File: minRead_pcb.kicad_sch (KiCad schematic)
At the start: 154 parts, among them J1 USB_C_Receptacle, J2 FH34SRJ-24S-0.5SH_50_, J3 FH34SRJ-6S-0.5SH_50_, J4 FH34SRJ-6S-0.5SH_50_, J5 Conn_01x02, J6 PPPC062LJBN-RC, J7 Micro_SD_Card, Q1 FS8205A, Q12 MMBT3904, Q13 MMBT3904, Q14 AO3419, Q15 MMBT3906, Q16 MMBT3906, Q17 MMBT3904, Q3 AO3419, Q4 BSS138, Q5 BSS138, Q6 BSS138, Q7 AO3419, Q8 AO3419, Q9 BSS138, SW1 SW_Push, SW10 SW_Push, SW11 SW_Push, SW2 SW_Push, SW3 SW_Push, SW4 SW_Push, SW5 SW_Push, SW6 SW_Push, SW7 SW_Push, SW8 SW_Push, SW9 SW_Push, U1 TPD4E1U06DBVR, U10 AP3031KTR, U2 TPS2116DRL, U3 AP2112K-3.3, U4 ESP32-S3-WROOM-1, U5 DW01A, U6 TPD4E1U06DBVR, U7 MCP73832-2-OT, U8 TPD4E1U06DBVR, U9 TPD4E1U06DBVR

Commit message: Schematic/PCB: finalize changes and layout progress
C- -> pin 1; W- -> pin 2; GND -> pin 3.

Schematic mostly finalized. 74 inverter used instead of PNP/NPN. ESP32 pinout configured. Components semi-optimally laid out; remaining traces TBD.
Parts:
- removed Q16: MMBT3906, Package_TO_SOT_SMD:SOT-23_Handsoldering, symbol Transistor_BJT:MMBT3906
- removed Q17: MMBT3904, Package_TO_SOT_SMD:SOT-23_Handsoldering, symbol Transistor_BJT:MMBT3904
- removed R47, R48: 18k, Resistor_SMD:R_0805_2012Metric_Pad1.20x1.40mm_HandSolder, symbol Device:R
- removed U7: MCP73832-2-OT, Package_TO_SOT_SMD:SOT-23-5, symbol Battery_Management:MCP73832-2-OT
- added R62: 10k, Resistor_SMD:R_0805_2012Metric_Pad1.20x1.40mm_HandSolder, symbol Device:R
- added R63, R64: 100, Resistor_SMD:R_0805_2012Metric_Pad1.20x1.40mm_HandSolder, symbol Device:R
- added R65: 33, Resistor_SMD:R_0805_2012Metric_Pad1.20x1.40mm_HandSolder, symbol Device:R
- added U11: TP4056-42-ESOP8, Package_SO:SOIC-8-1EP_3.9x4.9mm_P1.27mm_EP2.41x3.3mm_ThermalVias, symbol Battery_Management:TP4056-42-ESOP8
- added U12: 74LVC1G04, Package_TO_SOT_SMD:SOT-23-5_HandSoldering, symbol 74xGxx:74LVC1G04
- added U7: TPD4E1U06DBVR, Package_TO_SOT_SMD:SOT-23-6_Handsoldering, symbol TPD4E1U06DBVR:TPD4E1U06DBVR
- C2, C3: value 4.7u -> 10u
- C24: value 2.2n -> 100n
- D2: footprint LED_THT:LED_D3.0mm -> LED_SMD:LED_1206_3216Metric_Pad1.42x1.75mm_HandSolder
- R6: value 10k -> 12k
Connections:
- net CHG_STATUS is gone; now on net BAT_MONIT: U4.12 (IO8)
- net LED_PWR is gone; now on an unnamed net: U4.10 (IO17)
- net WARM_TOGGLE is gone; now on an unnamed net: U4.6 (IO6)
- net 3V3: now also C24.1, U12.5 (VCC)
- net BAT_MONIT: no longer U4.4 (IO4)
- net BUTTON_ADC_2: now also U4.4 (IO4); no longer U4.38 (IO2)
- net C-: now also Q6.3 (D), R49.1; no longer Q5.3 (D), R50.1
- net COLOR_SEL: now also U4.35 (IO42), U12.2
- net COLOR_SEL_INV: now also U12.4; no longer C24.1
- net ESP32_EN: now also R63.2; no longer SW11.2
- net ESP32_IO0: now also R64.2; no longer SW6.2
- net GND: now also C29.2, D8.3 (common), U11.1 (TEMP), U11.3 (GND), U11.9 (EPAD), U12.3 (GND), U7.2; no longer C29.1, D8.2 (common)
- net ISO_GATE: now also Q12.3 (C), Q9.1 (G), R42.2, R43.2
- net LED_ACTIVATE: now also U4.34 (IO41)
- net P+: now also U11.5 (BAT)
- net PWM_LED: now also U4.33 (IO40); no longer U4.5 (IO5)
- net PWR_BUTTON: now also C29.1, U4.11 (IO18), R62.2; no longer SW10.1, U4.15 (IO3)
- net RX: no longer J6.6, U9.4
- net SD_CLK: now also U9.1
- net SD_CMD: now also U9.3
- net SD_DAT0: now also U1.6; no longer U1.4
- net SD_DAT1: now also U1.4; no longer U1.3
- net SD_DAT2: now also U1.3; no longer U1.1
- net SD_DAT3: now also U1.1; no longer U1.6
- net TX: no longer J6.11, U8.3
- net USB_STAT: now also U4.17 (IO9)
- net USB_VBUS: now also U11.4 (V_{CC}), U11.8 (CE)
- net W-: now also D8.2 (A2), Q5.3 (D), R50.1; no longer D8.3 (A2), Q6.3 (D), R49.1
- net at R59.2: now also U11.7 (~{CHRG})
- net at R21.1: no longer U4.35 (IO42)
- net at R23.1: now also U4.8 (IO15); no longer U4.33 (IO40)
- net at R29.2: now also U4.20 (IO12); no longer U4.17 (IO9)
- net at R6.1: now also U11.2 (PROG)
- net at R33.2: now also U4.24 (IO47); no longer U4.21 (IO13)
- net at R22.1: now also U4.9 (IO16); no longer U4.34 (IO41)
- net at R26.1: now also U4.5 (IO5); no longer U4.25 (IO48)
- net at R25.1: now also U4.7 (IO7); no longer U4.32 (IO39)
- net at R24.1: no longer U4.31 (IO38)
- net at R32.2: now also U4.23 (IO21); no longer U4.20 (IO12)
- net at R34.2: now also U4.25 (IO48); no longer U4.22 (IO14)
- net at R30.2: now also U4.21 (IO13); no longer U4.18 (IO10)
- net at R31.2: now also U4.22 (IO14); no longer U4.19 (IO11)
- net EPD_MOSI renamed SPI_MOSI
- net EPD_SCK renamed SPI_SCK
- net INT renamed TP_INT
- net TP_INT: now also U4.18 (IO10), U7.1
- net RST renamed TP_RST
- net TP_RST: now also U4.19 (IO11), U7.3
- net SCL renamed I2C_SCL
- net I2C_SCL: now also U4.32 (IO39), U7.6
- net SDA renamed I2C_SDA
- net I2C_SDA: now also U4.31 (IO38), U7.4
- removed net UNUSED_GPIO_15: J6.5, U4.8 (IO15), U9.3
- removed net UNUSED_GPIO_16: J6.10, U4.9 (IO16), U9.6
- removed net UNUSED_GPIO_45: J6.3, U4.26 (IO45), U9.1
- removed net UNUSED_GPIO_46: J6.9, U4.16 (IO46), U8.6
- removed net UNUSED_GPIO_47: J6.4, U4.24 (IO47), U8.1
- new net: R62.1, SW10.1
- new net: R63.1, SW11.2
- new net: R65.2, U4.38 (IO2)
- new net: R64.1, SW6.2
- new net SPI_MISO: R65.1
- new net UNUSED_GPIO_3: U4.15 (IO3)
- no-connect marks 13 -> 15
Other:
- note added: "1u cap placed at ESP32"
- note added: "2.2n cap placed near ESP32"
- note added: "R6 12kohm -> 100mA charge rate"
- note removed: "10kohm -> 100mA charge rate"
- note removed: "Taken from"
- note removed: "https://tinyurl.com/4bm2ynx9"
- moved on the sheet: C2, C27, C8, D2, H1, H2, H3, H4, J4, R21, R22, R23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

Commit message: finished layout, schematic, tbd on next steps for review
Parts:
- SW6: footprint Button_Switch_THT:SW_PUSH_6mm -> Button_Switch_THT:SW_PUSH_1P1T_6x3.5mm_H4.3_APEM_MJTP1243; now fitted
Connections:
- net 3V3: now also J6.7; no longer J6.12
- net C-: now also J6.11; no longer J6.2
- net GND: now also J6.12
- net I2C_SCL: now also J6.10, U8.3
- net I2C_SDA: now also J6.4, U8.4
- net LED_SW: now also J6.5; no longer J6.7
- net SPI_MISO: now also J6.3, U8.1
- net SPI_MOSI: now also J6.8, U9.4
- net SPI_SCK: now also J6.2, U9.6
- net UNUSED_GPIO_3: now also J6.9, U8.6
- net W-: now also J6.6; no longer J6.8
- no-connect marks 15 -> 14

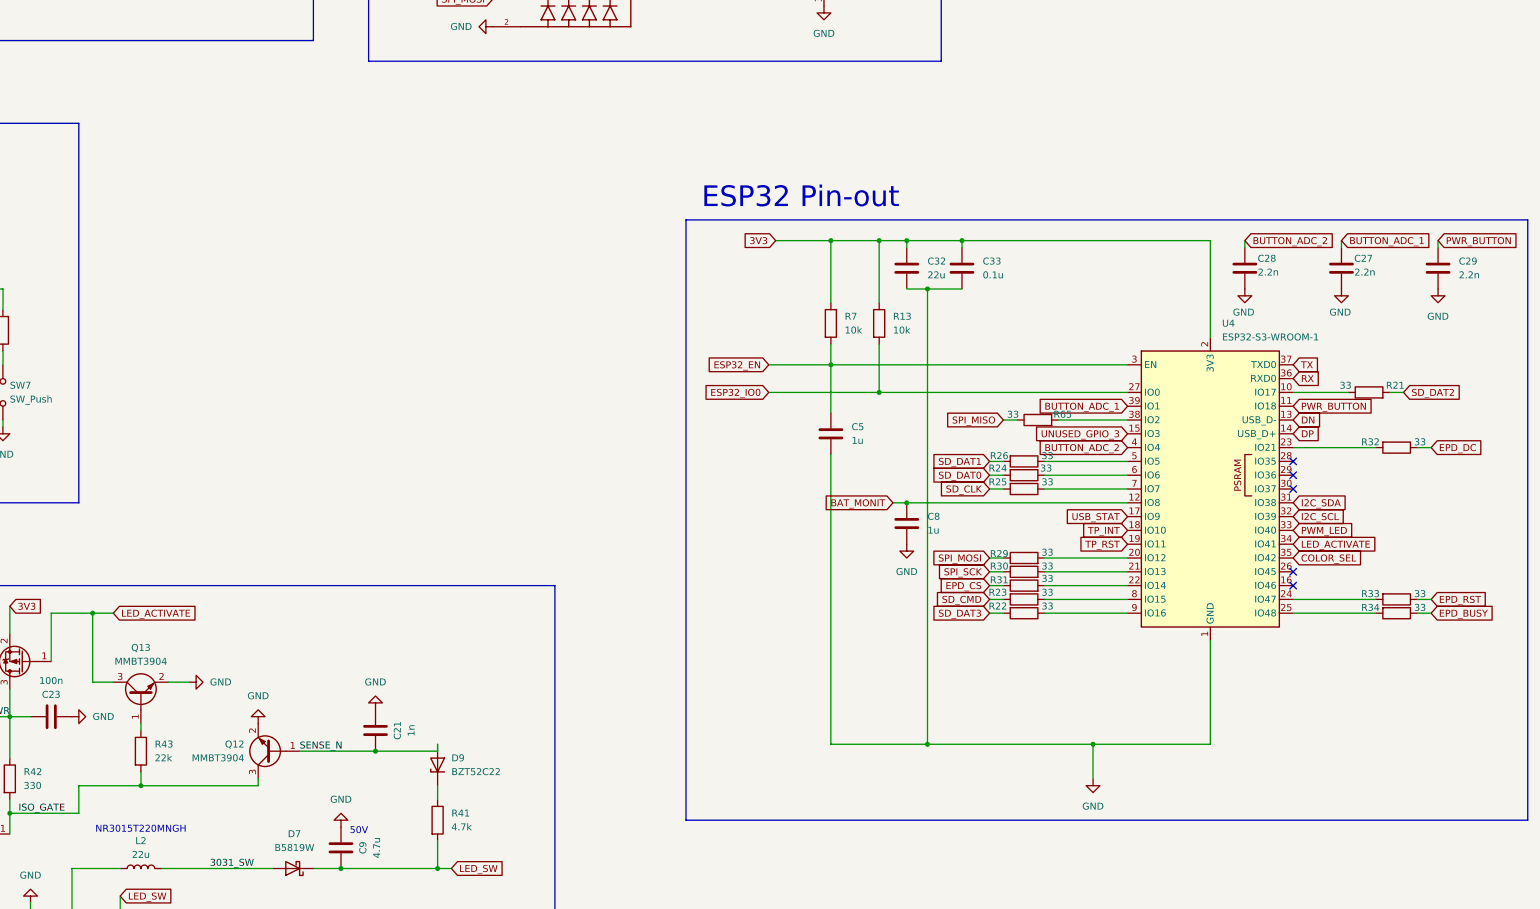
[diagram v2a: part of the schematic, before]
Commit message: removed (most) vias on pads, added rtc ds3231, added TPs for UART TX/RX TBD: trace spacing, further review of habits
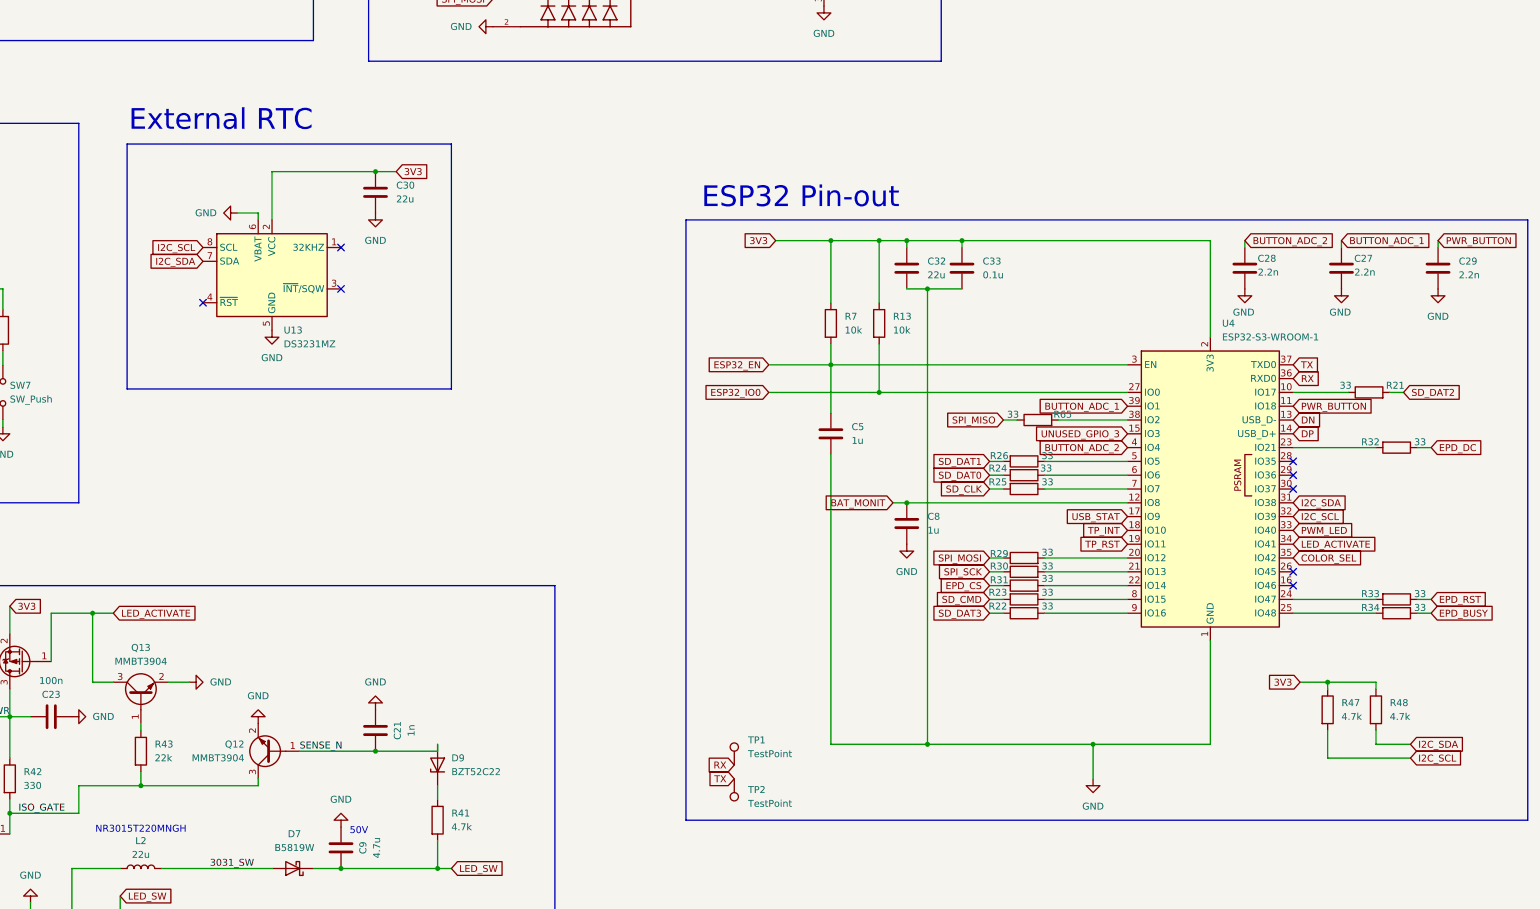
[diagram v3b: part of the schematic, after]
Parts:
- added C30: 22u, Capacitor_SMD:C_0805_2012Metric_Pad1.18x1.45mm_HandSolder, symbol Device:C
- added R47, R48: 4.7k, Resistor_SMD:R_0805_2012Metric_Pad1.20x1.40mm_HandSolder, symbol Device:R
- added TP1, TP2: TestPoint, TestPoint:TestPoint_Pad_1.0x1.0mm, symbol Connector:TestPoint
- added U13: DS3231MZ, Package_SO:SOIC-8_3.9x4.9mm_P1.27mm, symbol Timer_RTC:DS3231MZ
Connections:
- net 3V3: now also C30.1, R47.1, R48.1, U13.2 (VCC)
- net GND: now also C30.2, U13.5 (GND), U13.6 (VBAT)
- net I2C_SCL: now also R47.2, U13.8 (SCL)
- net I2C_SDA: now also R48.2, U13.7 (SDA)
- net RX: now also TP1.1
- net TX: now also TP2.1
- no-connect marks 14 -> 17
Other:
- note added: "External RTC"

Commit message: added voltage divider to 3031 reduced led driver passives size to 0603
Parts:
- added R66: 680k, Resistor_SMD:R_0603_1608Metric_Pad0.98x0.95mm_HandSolder, symbol Device:R
- added R67: 1M, Resistor_SMD:R_0603_1608Metric_Pad0.98x0.95mm_HandSolder, symbol Device:R
- C12, C21, C23, C24: footprint Capacitor_SMD:C_0805_2012Metric_Pad1.18x1.45mm_HandSolder -> Capacitor_SMD:C_0603_1608Metric_Pad1.08x0.95mm_HandSolder
- R17, R37, R39, R40, R41, R42, R43, R44, R45, R46, R49, R50, R52: footprint Resistor_SMD:R_0805_2012Metric_Pad1.20x1.40mm_HandSolder -> Resistor_SMD:R_0603_1608Metric_Pad0.98x0.95mm_HandSolder
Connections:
- net GND: now also R67.2
- net LED_SW: now also R66.1; no longer U10.5 (OV)
- new net OVP: R66.2, R67.1, U10.5 (OV)

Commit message: updated silkscreen reference spacing updated silkscreen of graphics still need to do more of above added netclass for switching nodes and high voltage output caps, enforced 3mm clearance
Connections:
- net EINK_SW: now reaches C11.2, D5.2 (A), L1.1, Q4.3 (D)
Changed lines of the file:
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@@
 		)
 	)
-	(label "3031_SW"
-		(at 289.56 312.42 0)
-		(effects
-			(font
-				(size 1.27 1.27)
-			)
-			(justify left bottom)
-		)
-	)
 	(label "LATCH_PWR"
 		(at 278.13 248.92 180)
@@
 		)
 	)
-	(label "3031_SW"
-		(at 314.96 276.86 0)
-		(effects
-			(font
-				(size 1.27 1.27)
-			)
-			(justify left bottom)
-		)
-	)
 	(label "GDR"
 		(at 140.97 251.46 180)
@@
 		)
 	)
+	(global_label "3031_SW"
+		(shape input)
+		(at 318.77 276.86 90)
+		(fields_autoplaced yes)
+		(effects
+			(font
+				(size 1.27 1.27)
+			)
+			(justify left)
+		)
+		(property "Intersheetrefs" "${INTERSHEET_REFS}"
+			(at 318.77 265.4083 90)
+			(effects
+				(font
+					(size 1.27 1.27)
+				)
+				(justify left)
+				(hide yes)
+			)
+		)
+	)
 	(global_label "COLOR_SEL"
 		(shape input)
@@
 		)
 	)
+	(global_label "3031_SW"
+		(shape input)
+		(at 289.56 312.42 180)
+		(fields_autoplaced yes)
+		(effects
+			(font
+				(size 1.27 1.27)
+			)
+			(justify right)
+		)
+		(property "Intersheetrefs" "${INTERSHEET_REFS}"
+			(at 278.1083 312.42 0)
+			(effects
+				(font
+					(size 1.27 1.27)
+				)
+				(justify right)
+				(hide yes)
+			)
+		)
+	)
 	(global_label "3V3"
 		(shape input)
@@
 				(hide yes)
 			)
+		)
+	)
+	(global_label "EINK_SW"
+		(shape input)
+		(at 66.04 294.64 0)
+		(fields_autoplaced yes)
+		(effects
+			(font
+				(size 1.27 1.27)
+			)
+			(justify left)
+		)
+		(property "Intersheetrefs" "${INTERSHEET_REFS}"
+			(at 77.008 294.64 0)
+			(effects
+				(font
+					(size 1.27 1.27)
+				)
+				(justify left)
+				(hide yes)
+			)

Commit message: - added LED_ACTIVATE net to proper spot for transistor latch mechanism - added moved 1M ground bleed to SENSE_N instead of 3V3 - removed SPI signals from external header - added GPIO3, GPIO46, GPIO2 to external header with 33ohm series resistors - added P+ to external header with TS05D ESD protection diode - replaced inductor with molded inductor for LED driver (noise reduction) - replaced output cap for LED driver with tantalum cap (noise reduction) - cleaned up unconnected nets - todo: silkscreen (again), EMI stuff, etc
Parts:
- added CR3: TSD05CDYFR, Diode_SMD:D_SOD-323_HandSoldering, symbol TSD05CDYFR:TSD05CDYFR
- added R68, R69: 33, Resistor_SMD:R_0805_2012Metric_Pad1.20x1.40mm_HandSolder, symbol Device:R
- C30: value 22u -> 0.1u
- C9: value 4.7u -> 1u; footprint Capacitor_SMD:C_0805_2012Metric_Pad1.18x1.45mm_HandSolder -> Capacitor_Tantalum_SMD:CP_EIA-3528-21_Kemet-B_HandSolder; symbol Device:C -> Device:C_Polarized
- L2: value 22u -> 4.7u; footprint srn3010C-100m:IND_SRN3010C-100M -> Inductor_SMD:L_1008_2520Metric_Pad1.43x2.20mm_HandSolder
- R40: value 10k -> 100k
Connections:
- net 3V3: now also U13.6 (VBAT); no longer R17.1, U13.2 (VCC)
- net GND: now also C9.2, U13.2 (VCC), CR3.2 (GND); no longer C9.1, U13.6 (VBAT)
- net LED_ACTIVATE: now also Q9.2 (S), R39.1
- net LED_SW: now also C9.1; no longer C9.2
- net P+: now also J6.8, CR3.1 (I/O)
- net SENSE_N: now also R17.1
- net SPI_MISO: now also U4.26 (IO45); no longer J6.3, R65.1, U8.1
- net SPI_MOSI: no longer J6.8, U9.4
- net SPI_SCK: no longer J6.2, U9.6
- net UNUSED_GPIO_3: now also R68.1; no longer U4.15 (IO3)
- net at U4.16 (IO46): now also R69.1
- new net: R68.2, U4.15 (IO3)
- new net UNUSED_GPIO_2: J6.3, R65.1, U8.1
- new net UNUSED_GPIO_46: J6.2, R69.2, U9.6
- no-connect marks 17 -> 16
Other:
- note added: "50V Tantalum"
- note added: "74479325207247"
- note removed: "50V"
- moved on the sheet: C30, D9, R17, R65

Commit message: Swap AP3031 -> TPS923610DRLR, add SW net-class
- add SW net-class and assignments (3031_SW, LED_SW, EINK_SW) in .kicad_pro
- remove AP3031 symbol library (AP3031.kicad_sym/.bak) + sym-lib-table entry
- add TPS923610DRLR: symbol, footprint (U_DRL0006A_6L_TEX + L/M variants),
  and SOT563 3D model; registered in sym-lib-table and fp-lib-table
- schematic/board design updates
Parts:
- removed C9: 1u, Capacitor_Tantalum_SMD:CP_EIA-3528-21_Kemet-B_HandSolder, symbol Device:C_Polarized
- removed D7: B5819W, Diode_SMD:D_SOD-123, symbol Diode:MBR0540
- removed D9: BZT52C22, Diode_SMD:D_SOD-123F, symbol Diode:BZT52Bxx
- removed Q12, Q13: MMBT3904, Package_TO_SOT_SMD:SOT-23_Handsoldering, symbol Transistor_BJT:MMBT3904
- removed Q14: AO3419, Package_TO_SOT_SMD:SOT-23_Handsoldering, symbol Transistor_FET:IRLML6402
- removed Q15: MMBT3906, Package_TO_SOT_SMD:SOT-23_Handsoldering, symbol Transistor_BJT:MMBT3906
- removed Q9: BSS138, Package_TO_SOT_SMD:SOT-23, symbol Transistor_FET:BSS138
- removed U10: AP3031KTR, Package_TO_SOT_SMD:SOT-23-6_Handsoldering, symbol AP3031:AP3031KTR
- added C31: 10n, Capacitor_SMD:C_0805_2012Metric_Pad1.18x1.45mm_HandSolder, symbol Device:C
- added C9: 1u, Capacitor_SMD:C_0805_2012Metric_Pad1.18x1.45mm_HandSolder, symbol Device:C
- added R70: 100k, Resistor_SMD:R_0805_2012Metric_Pad1.20x1.40mm_HandSolder, symbol Device:R
- added R71: 22k, Resistor_SMD:R_0805_2012Metric_Pad1.20x1.40mm_HandSolder, symbol Device:R
- added R72: 10k, Resistor_SMD:R_0805_2012Metric_Pad1.20x1.40mm_HandSolder, symbol Device:R
- added R73, R74: 0, Resistor_SMD:R_0805_2012Metric_Pad1.20x1.40mm_HandSolder, symbol Device:R
- added TP3, TP4, TP5: TestPoint, Connector_PinHeader_2.54mm:PinHeader_1x01_P2.54mm_Vertical, symbol Connector:TestPoint
- added U10: TPS923610DRLR, TPS923610DRLR:U_DRL0006A_6L_TEX-M, symbol TPS923610DRLR:TPS923610DRLR
- C12, C24: footprint Capacitor_SMD:C_0603_1608Metric_Pad1.08x0.95mm_HandSolder -> Capacitor_SMD:C_0805_2012Metric_Pad1.18x1.45mm_HandSolder
- C21: value 1n -> 1u; footprint Capacitor_SMD:C_0603_1608Metric_Pad1.08x0.95mm_HandSolder -> Capacitor_SMD:C_0805_2012Metric_Pad1.18x1.45mm_HandSolder
- C23: value 100n -> 2.2n; footprint Capacitor_SMD:C_0603_1608Metric_Pad1.08x0.95mm_HandSolder -> Capacitor_SMD:C_0805_2012Metric_Pad1.18x1.45mm_HandSolder
- R17: value 1M -> 100k; footprint Resistor_SMD:R_0603_1608Metric_Pad0.98x0.95mm_HandSolder -> Resistor_SMD:R_0805_2012Metric_Pad1.20x1.40mm_HandSolder
- R37, R40, R49, R50: footprint Resistor_SMD:R_0603_1608Metric_Pad0.98x0.95mm_HandSolder -> Resistor_SMD:R_0805_2012Metric_Pad1.20x1.40mm_HandSolder
- R39: value 100k -> 1M; footprint Resistor_SMD:R_0603_1608Metric_Pad0.98x0.95mm_HandSolder -> Resistor_SMD:R_0805_2012Metric_Pad1.20x1.40mm_HandSolder
- R41: value 4.7k -> 120k; footprint Resistor_SMD:R_0603_1608Metric_Pad0.98x0.95mm_HandSolder -> Resistor_SMD:R_0805_2012Metric_Pad1.20x1.40mm_HandSolder
- R42: value 330 -> 0; footprint Resistor_SMD:R_0603_1608Metric_Pad0.98x0.95mm_HandSolder -> Resistor_SMD:R_0805_2012Metric_Pad1.20x1.40mm_HandSolder
- R43: value 22k -> 0; footprint Resistor_SMD:R_0603_1608Metric_Pad0.98x0.95mm_HandSolder -> Resistor_SMD:R_0805_2012Metric_Pad1.20x1.40mm_HandSolder; now not fitted; now left out of the parts list
- R44: value 10k -> 0; footprint Resistor_SMD:R_0603_1608Metric_Pad0.98x0.95mm_HandSolder -> Resistor_SMD:R_0805_2012Metric_Pad1.20x1.40mm_HandSolder
- R45: value 10k -> 0; footprint Resistor_SMD:R_0603_1608Metric_Pad0.98x0.95mm_HandSolder -> Resistor_SMD:R_0805_2012Metric_Pad1.20x1.40mm_HandSolder; now not fitted; now left out of the parts list
- R46: value 47k' -> 0; footprint Resistor_SMD:R_0603_1608Metric_Pad0.98x0.95mm_HandSolder -> Resistor_SMD:R_0805_2012Metric_Pad1.20x1.40mm_HandSolder
- R52: value 22k -> 0; footprint Resistor_SMD:R_0603_1608Metric_Pad0.98x0.95mm_HandSolder -> Resistor_SMD:R_0805_2012Metric_Pad1.20x1.40mm_HandSolder
- R58: value 100k -> 0; now not fitted; now left out of the parts list
- R59: value 1k -> 2k
- R66: value 680k -> 0; footprint Resistor_SMD:R_0603_1608Metric_Pad0.98x0.95mm_HandSolder -> Resistor_SMD:R_0805_2012Metric_Pad1.20x1.40mm_HandSolder; now not fitted; now left out of the parts list
- R67: value 1M -> 56k; footprint Resistor_SMD:R_0603_1608Metric_Pad0.98x0.95mm_HandSolder -> Resistor_SMD:R_0805_2012Metric_Pad1.20x1.40mm_HandSolder
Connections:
- net 3031_SW: now also U10.6 (SW)
- net 3V3: now also C21.1, R42.1, R66.1, R70.2, R74.1; no longer J4.2, R39.2, R58.2
- net GND: now also C21.2, R41.2, R59.2, C31.2, C9.1, R73.1, U10.4 (GND); no longer C21.1, R17.2, R52.1, R67.2, SW7.1
- net I2C_SCL: now also R45.1, R52.1; no longer J4.6, U7.6
- net I2C_SDA: now also R46.1, R58.1; no longer J4.5, U7.4
- net LED_ACTIVATE: now also Q7.1 (G), R40.1; no longer R39.1
- net LED_SW: now also R39.1, C9.2, U10.5 (VOUT); no longer R41.2, R66.1
- net PWM_LED: now also U10.2 (ADIM)
- net PWR_BUTTON: now also R72.1
- net TP_INT: now also R43.1, R44.1; no longer J4.4, U7.1
- net UNUSED_GPIO_46: now also R65.2; no longer R69.2
- net USB_STAT: now also C23.1, R17.2, R67.2, U4.38 (IO2), R70.1, R71.2; no longer R58.1, U2.8 (ST), U4.17 (IO9)
- net CHRG: now reaches U11.7 (~{CHRG})
- net CHRG: now also R67.1; no longer R59.2
- net at C12.2, L2.1, Q7.3 (D): now also U10.1 (VIN); no longer R52.2
- net at Q5.2 (S), Q6.2 (S), R37.1: now also U10.3 (FB)
- net at U4.16 (IO46): now also R65.1; no longer R69.1
- net PIN_6: now reaches R45.2
- net PIN_6: now also J4.6, R52.2, U7.6; no longer R46.1
- net PIN_4: now reaches R44.2
- net PIN_4: now also J4.4, R66.2, U7.1
- net LED_MONIT: now reaches R41.1
- net LED_MONIT: now also R39.2, U4.17 (IO9), C31.1
- net STDBY: now reaches U11.6 (~{STDBY})
- net STDBY: now also R71.1
- net IO35_PSRAM: now reaches U4.28 (IO35)
- net IO35_PSRAM: now also TP5.1
- net IO36_PSRAM: now reaches U4.29 (IO36)
- net IO36_PSRAM: now also TP4.1
- net IO37_PSRAM: now reaches U4.30 (IO37)
- net IO37_PSRAM: now also TP3.1
- net at R36.1, SW7.2: now also R72.2
- net ISO_GATE renamed PIN_2
- net PIN_2: now also J4.2; no longer R45.1
- removed net LATCH_PWR: C23.1, R42.1, R46.2
- removed net OVP: R66.2, R67.1
- removed net SENSE_N: C21.2, R17.1, R44.1
- net SPI_MISO: no longer names the net of U4.26 (IO45)
- net SPI_MISO: now also R69.1
- net UNUSED_GPIO_2 renamed UNUSED_GPIO_45
- net UNUSED_GPIO_45: now also R69.2; no longer R65.1
- new net: R73.2, R74.2, SW7.1
- new net PIN_5: J4.5, R46.2, R58.2, U7.4
- new net ST: R17.1, U2.8 (ST)
- no-connect marks 16 -> 12
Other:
- note added: "50V"
- note added: "Alternate Configuration (rarely used, do not populate by default)"
- note added: "ESP32-S31-WROOM-1 does not reserve GPIO for PSRAM Future proofing :)"
- note added: "LED lit when plugged in 2.5mA at 2.0Vf (5 − 2.0)/0.0015 ≈ 2 kΩ"
- note added: "Touch Connector + ESD"
- note added: "Touch Jumper Mux"
- note added: "Typical Configuration used on 4.26""
- note added: "UP(2) can serve as a power button if R36/R73 are unpopulated and R72/R74 are populated"
- note added: "USB / CHARGE STATUS ADC DIVIDER NOTE: Monitors TPS2116 ST and TP4056 CHRG/STDBY via single ADC pin (USB_STAT). Max continuous current draw: < 30 uA. PRIMARY OPERATIONAL STATES: 1) Discharging / Unplugged (VIN2 Active): ~1.98 V [Window: 1.70 V - 2.20 V] 2) Plugged in & Actively Charging: ~1.18 V [Window: 1.00 V - 1.35 V] 3) Plugged in & Fully Charged (Done): ~0.59 V [Window: 0.50 V - 0.70 V] 4) Pl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"
- note added: "USB Status"
- note removed: "2.5mA at 2.0Vf 4.6 - 2.0 / (0.0025) = 1kohm"
- note removed: "50V Tantalum"
- note removed: "Touch Connector"
- moved on the sheet: C12, C24, C30, C6, C8, D2, J3, J4, L2, Q5, Q6, Q7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
